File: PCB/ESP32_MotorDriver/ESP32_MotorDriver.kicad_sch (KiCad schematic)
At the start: 39 parts, among them J1 USB_C_Receptacle_USB2.0, J2 Conn_01x06, J4 Conn_01x05, J6 Conn_01x07, J7 Conn_01x17, Q1 SSM3J338R_LF, SW1 EN, SW2 BOOT, U1 ESP32-S2-SOLO-N4, U2 D3V3XA4B10LP, U4 TB6612FNG, U5 AP63203WU

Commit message: actual _v01
Issue with files being copied - these should be good
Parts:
- removed Q1: SSM3J338R_LF, SSM3J338R_LF:SOT-23F_TOS, symbol KiCADv6:SSM3J338R_LF
- removed R10, R9: 4k7, Resistor_SMD:R_0402_1005Metric_Pad0.72x0.64mm_HandSolder, symbol Device:R
- removed U2: D3V3XA4B10LP, Package_DFN_QFN:Diodes_UDFN-10_1x2.5mm_P0.5mm, symbol Power_Protection:D3V3XA4B10LP
- added D3: SMAJ12A, Diode_SMD:D_SMA, symbol Diode:SMAJ12A
- added F2: Polyfuse 500mA, Fuse:Fuse_0805_2012Metric_Pad1.15x1.40mm_HandSolder, symbol Device:Polyfuse
- added Q1: AO3407A, Package_TO_SOT_SMD:SOT-23, symbol Transistor_FET:AO3401A
- added R5, R6: 22R, Resistor_SMD:R_0402_1005Metric_Pad0.72x0.64mm_HandSolder, symbol Device:R_Small
- added U2: USBLC6-2SC6, Package_TO_SOT_SMD:SOT-23-6, symbol Power_Protection:USBLC6-2SC6
- C1, C11, C15, C3, C5, C7: MANUFACTURER (none) -> Samsung Electro-Mechanics; PN_Digikey (none) -> 1276-2891-1-ND; PN_LCSC (none) -> C15850; PN_Manufacturer (none) -> CL21A106KAYNNNE
- C10, C9: MANUFACTURER (none) -> Samsung Electro-Mechanics; PN_Digikey (none) -> 1276-2908-1-ND; PN_LCSC (none) -> C45783; PN_Manufacturer (none) -> CL21A226MAQNNNE
- C12, C13, C14, C2, C4, C6, C8: MANUFACTURER (none) -> Murata; PN_Digikey (none) -> 490-10700-1-ND; PN_LCSC (none) -> C77020; PN_Manufacturer (none) -> GRM155R71H104KE14D
- D1, D2: value D_Schottky -> SS14HE; PN_LCSC (none) -> C894424
- F1: value Polyfuse 4A -> Polyfuse 3A; footprint Fuse:Fuse_0805_2012Metric_Pad1.15x1.40mm_HandSolder -> Fuse:Fuse_1812_4532Metric_Pad1.30x3.40mm_HandSolder; LCSC PN C22368431 -> (none); MANUFACTURER (none) -> Bourns; PN_Digikey MFU08054.00CT-ND -> MF-MSMF250-16X-2CT-ND; PN_LCSC C22368431 -> C210838; PN_Manufacturer MFU0805FF04000P100 -> MF-MSMF250/16X-2
- J1: PN_LCSC (none) -> C165948
- L1: MANUFACTURER (none) -> Murata; Manufacturer Murata Electronics -> (none); PN_LCSC (none) -> C668313
- R1, R2: MANUFACTURER (none) -> Yageo; PN_Digikey (none) -> 311-5.10KLRCT-ND; PN_LCSC (none) -> C25905; PN_Manufacturer (none) -> RC0402FR-075K1L
- R11, R12, R3, R4: MANUFACTURER (none) -> Yageo; PN_Digikey (none) -> 311-10.0KLRCT-ND; PN_LCSC (none) -> C25744; PN_Manufacturer (none) -> RC0402FR-0710KL
- SW1: value EN -> RESET; MANUFACTURER (none) -> Mitsumi; PN_LCSC (none) -> C4364645
- SW2: MANUFACTURER (none) -> Mitsumi; PN_LCSC (none) -> C4364645
- U1: MAXIMUM_PACKAGE_HEIGHT (none) -> 3.25 mm; PN_Manufacturer (none) -> ESP32-S2-SOLO-N4
- U4: MANUFACTURER (none) -> Toshiba
- U5: MANUFACTURER (none) -> Diodes Incorporated; PN_LCSC (none) -> C780769
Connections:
- net GND: now also D3.2 (A2), U2.2 (GND)
- net USB_N: now also R5.1, U2.1 (I/O1), U2.6 (I/O1); no longer U1.13 (IO19)
- net USB_P: now also R6.1, U2.3 (I/O2), U2.4 (I/O2); no longer U1.14 (IO20)
- net VBUS: now also F2.2, U2.5 (VBUS); no longer J1.A4 (VBUS), J1.A9 (VBUS), J1.B4 (VBUS), J1.B9 (VBUS)
- net VM: now also D3.1 (A1)
- net Vbatt: now also Q1.3 (D)
- net at R11.2: now also Q1.1 (G)
- net at F1.1: now also Q1.2 (S)
- net MISO renamed IO12
- net MOSI renamed IO13
- net SCK renamed IO11
- net SCL renamed IO33
- net SDA renamed IO34
- new net: F2.1, J1.A4 (VBUS), J1.A9 (VBUS), J1.B4 (VBUS), J1.B9 (VBUS)
- new net USB_N_ESP: R5.2, U1.13 (IO19)
- new net USB_P_ESP: R6.2, U1.14 (IO20)
- no-connect marks 2 -> 4
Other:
- note removed: "I2C"
- moved on the sheet: R11

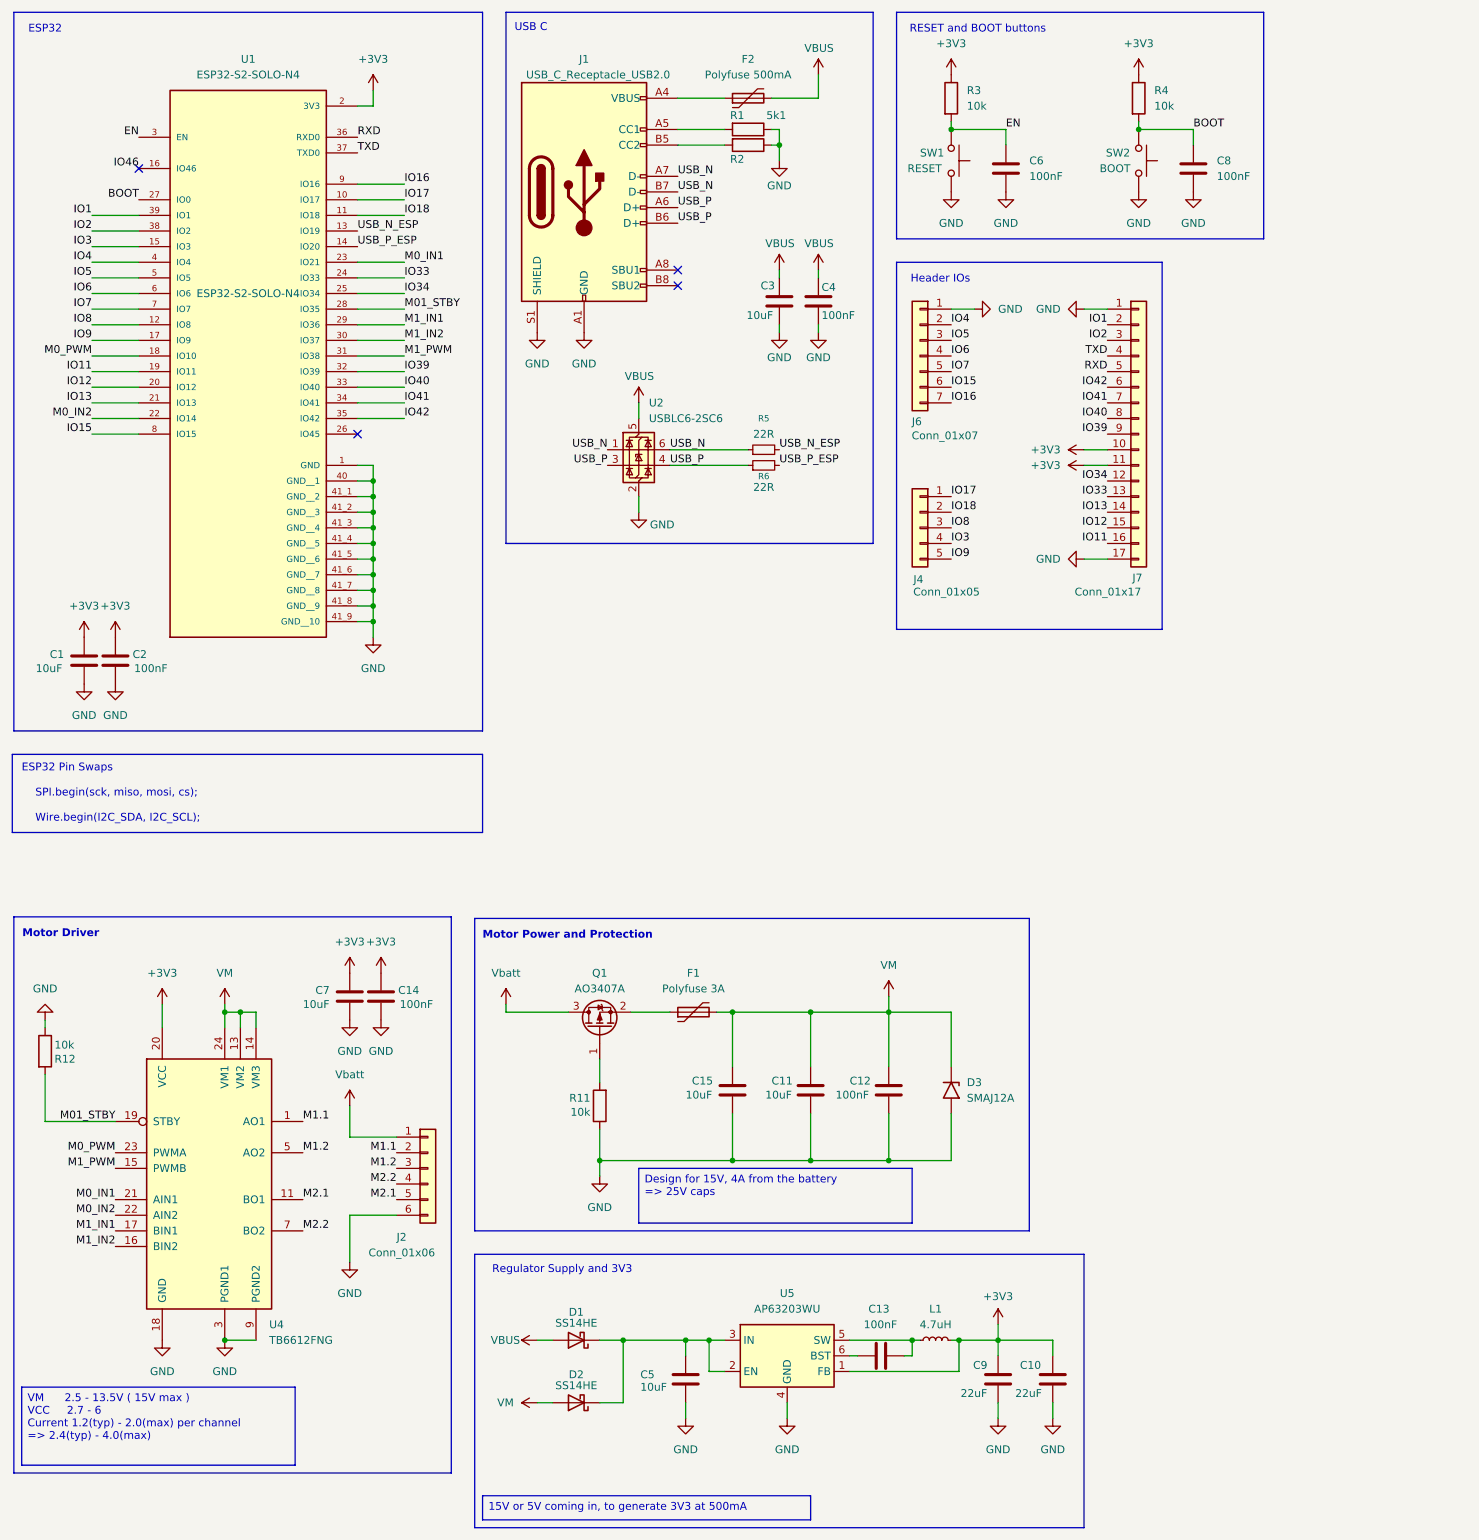
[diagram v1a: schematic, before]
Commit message: BOB v02
Submitted for manufacturer with a few minor fixes from v01. 3V3 to LineFollower array, New footprint for Motor connections and a switch added for power on/off
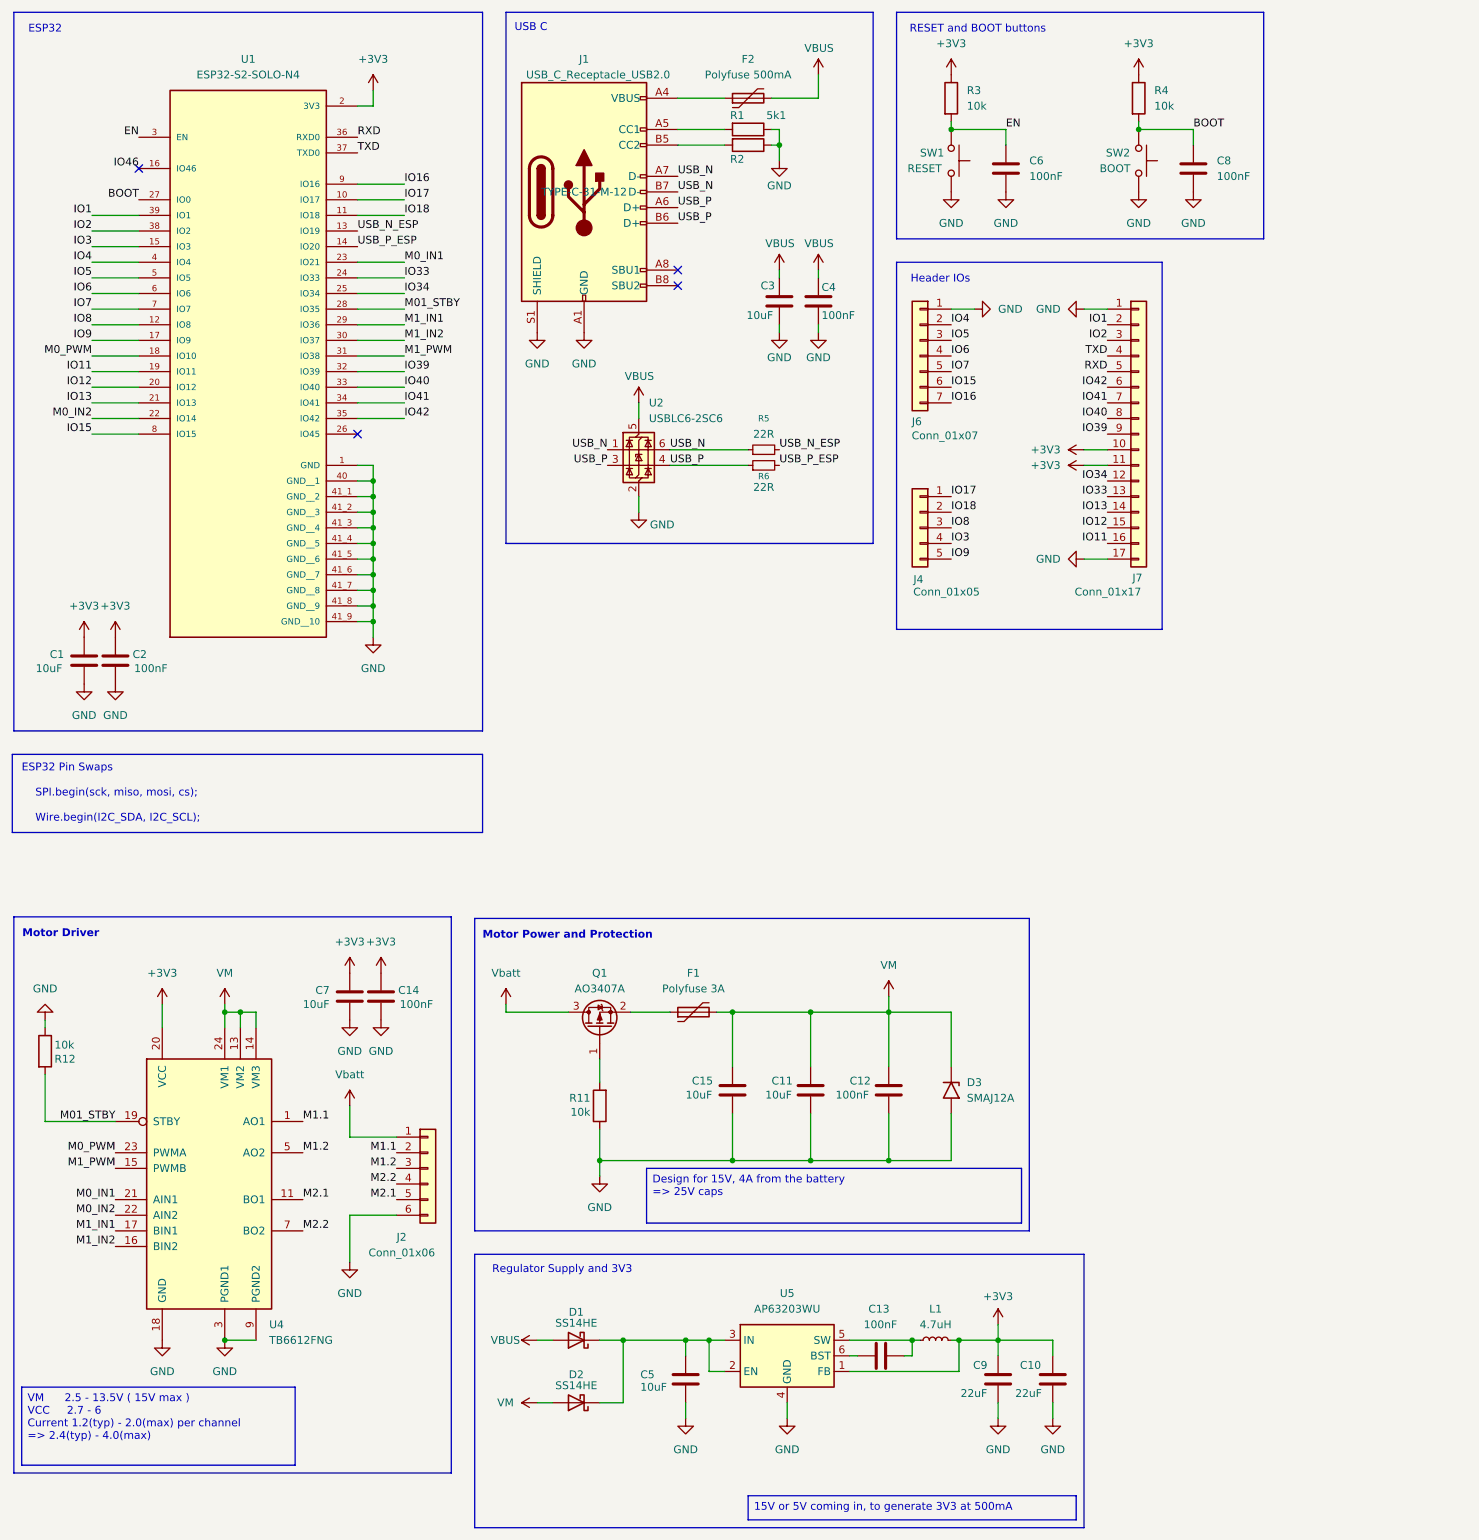
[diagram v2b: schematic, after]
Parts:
- D1, D2: footprint Diode_SMD:D_SOD-323F -> _diodes:D_SOD-323HE_SS14HE
- J1: MANUFACTURER (none) -> Korean Hroparts Elec; PN_Manufacturer (none) -> TYPE-C-31-M-12
- J2: MANUFACTURER (none) -> Adam Tech; PN_Digikey (none) -> 2057-PH1-06-UA-ND; PN_LCSC (none) -> C5845077; PN_Manufacturer (none) -> PH1-06-UA
- J4: MANUFACTURER (none) -> Adam Tech; PN_Digikey (none) -> 2057-PH1-05-UA-ND; PN_LCSC (none) -> C5374051; PN_Manufacturer (none) -> PH1-05-UA
- J6: MANUFACTURER (none) -> Adam Tech; PN_Digikey (none) -> 2057-PH1-07-UA-ND; PN_LCSC (none) -> C3331618; PN_Manufacturer (none) -> PH1-07-UA
- J7: MANUFACTURER (none) -> Adam Tech; PN_Digikey (none) -> 2057-PH1-17-UA-ND; PN_LCSC (none) -> C6251621; PN_Manufacturer (none) -> PH1-17-UA
- L1: MANUFACTURER Murata -> (none)
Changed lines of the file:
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@@
 	(text_box "15V or 5V coming in, to generate 3V3 at 500mA"
 		(exclude_from_sim no)
-		(at 93.98 258.9651 0)
+		(at 137.16 258.9651 0)
 		(size 53.34 3.9249)
 		(margins 0.9525 0.9525 0.9525 0.9525)
@@
 	(text_box "Design for 15V, 4A from the battery\n => 25V caps"
 		(exclude_from_sim no)
-		(at 119.38 205.74 0)
-		(size 44.45 8.89)
+		(at 120.65 205.74 0)
+		(size 60.96 8.89)
 		(margins 0.9525 0.9525 0.9525 0.9525)
 		(stroke
@@
 			)
 		)
-		(property "PN_Manufacturer" ""
+		(property "PN_Manufacturer" "TYPE-C-31-M-12"
 			(at 110.49 46.99 0)
 			(show_name no)
@@
 			)
 		)
+		(property "MANUFACTURER" "Korean Hroparts Elec"
+			(at 110.49 46.99 0)
+			(hide yes)
+			(show_name no)
+			(do_not_autoplace no)
+			(effects
+				(font
+					(size 1.27 1.27)
+				)
+			)
+		)
 		(pin "A1"
 		)
@@
 			)
 		)
-		(property "MANUFACTURER" "Murata"
-			(at 167.64 233.68 90)
-			(hide yes)
-			(show_name no)
-			(do_not_autoplace no)
-			(effects
-				(font
-					(size 1.27 1.27)
-				)
-			)
-		)
 		(pin "1"
 		)
@@
 			)
 		)
-		(property "Footprint" "Diode_SMD:D_SOD-323F"
+		(property "Footprint" "_diodes:D_SOD-323HE_SS14HE"
 			(at 109.22 243.84 0)
 			(hide yes)
@@
 			)
 		)
-		(property "PN_Manufacturer" ""
+		(property "PN_Manufacturer" "PH1-06-UA"
 			(at 85.09 205.74 0)
+			(hide yes)
 			(show_name no)
 			(do_not_autoplace no)
@@
 			)
 		)
-		(property "PN_Digikey" ""
+		(property "PN_Digikey" "2057-PH1-06-UA-ND"
 			(at 85.09 205.74 0)
 			(hide yes)
@@
 			)
 		)
+		(property "MANUFACTURER" "Adam Tech"
+			(at 85.09 205.74 0)
+			(hide yes)
+			(show_name no)
+			(do_not_autoplace no)
+			(effects
+				(font
+					(size 1.27 1.27)
+				)
+			)
+		)
+		(property "PN_LCSC" "C5845077"
+			(at 85.09 205.74 0)
+			(hide yes)
+			(show_name no)
+			(do_not_autoplace no)
+			(effects
+				(font
+					(size 1.27 1.27)
+				)
+			)
+		)
 		(pin "6"
 		)
@@
 			)
 		)
-		(property "PN_Manufacturer" ""
+		(property "PN_Manufacturer" "PH1-05-UA"
 			(at 165.1 101.6 0)
+			(hide yes)
 			(show_name no)
 			(do_not_autoplace no)
@@
 			)
 		)
-		(property "PN_Digikey" ""
+		(property "PN_Digikey" "2057-PH1-05-UA-ND"
+			(at 165.1 101.6 0)
+			(hide yes)
+			(show_name no)
+			(do_not_autoplace no)
+			(effects
+				(font
+					(size 1.27 1.27)
+				)
+			)
+		)
+		(property "MANUFACTURER" "Adam Tech"
+			(at 165.1 101.6 0)
+			(hide yes)
+			(show_name no)
+			(do_not_autoplace no)
+			(effects
+				(font
+					(size 1.27 1.27)
+				)
+			)
+		)
+		(property "PN_LCSC" "C5374051"
 			(at 165.1 101.6 0)
 			(hide yes)
@@
 			)
 		)
-		(property "PN_Manufacturer" ""
+		(property "PN_Manufacturer" "PH1-07-UA"
 			(at 165.1 73.66 0)
+			(hide yes)
 			(show_name no)
 			(do_not_autoplace no)
@@
 			)
 		)
-		(property "PN_Digikey" ""
+		(property "PN_Digikey" "2057-PH1-07-UA-ND"
 			(at 165.1 73.66 0)
 			(hide yes)
@@
 			)
 		)
+		(property "MANUFACTURER" "Adam Tech"
+			(at 165.1 73.66 0)
+			(hide yes)
+			(show_name no)
+			(do_not_autoplace no)
+			(effects
+				(font
+					(size 1.27 1.27)
+				)
+			)
+		)
+		(property "PN_LCSC" "C3331618"
+			(at 165.1 73.66 0)
+			(hide yes)
+			(show_name no)
+			(do_not_autoplace no)
+			(effects
+				(font
+					(size 1.27 1.27)
+				)
+			)
+		)
 		(pin "1"
 		)
@@
 			)
 		)
-		(property "Footprint" "Diode_SMD:D_SOD-323F"
+		(property "Footprint" "_diodes:D_SOD-323HE_SS14HE"
 			(at 109.22 233.68 0)
 			(hide yes)
@@
 			)
 		)
-		(property "PN_Manufacturer" ""
+		(property "PN_Manufacturer" "PH1-17-UA"
 			(at 200.66 86.36 0)
+			(hide yes)
 			(show_name no)
 			(do_not_autoplace no)
@@
 			)
 		)
-		(property "PN_Digikey" ""
+		(property "PN_Digikey" "2057-PH1-17-UA-ND"
+			(at 200.66 86.36 0)
+			(hide yes)
+			(show_name no)
+			(do_not_autoplace no)
+			(effects
+				(font
+					(size 1.27 1.27)
+				)
+			)
+		)
+		(property "MANUFACTURER" "Adam Tech"
+			(at 200.66 86.36 0)
+			(hide yes)
+			(show_name no)
+			(do_not_autoplace no)
+			(effects
+				(font
+					(size 1.27 1.27)
+				)
+			)
+		)
+		(property "PN_LCSC" "C6251621"
 			(at 200.66 86.36 0)
 			(hide yes)
@@
 		(property "PN_Manufacturer" "ESP32-S2-SOLO-N4"
 			(at 55.88 63.5 0)
+			(hide yes)
 			(show_name no)
 			(do_not_autoplace no)
@@
 			(at 113.03 195.58 0)
 			(hide yes)
-			(show_name no)
-			(do_not_autoplace no)
-			(effects
-				(font
-					(size 1.27 1.27)
-				)
-			)
-		)
-		(property "Supplier" ""
-			(at 113.03 195.58 0)
-			(hide yes)
-			(show_name no)
-			(do_not_autoplace no)
-			(effects
-				(font
-					(size 1.27 1.27)
-				)
-			)
-		)
-		(property "PN_Digikey_150mA" ""
-			(at 113.03 195.58 0)
-			(hide yes)
-			(show_name no)
-			(do_not_autoplace no)
-			(effects
-				(font
-					(size 1.27 1.27)
-				)
-			)
-		)
-		(property "PN_Digikey_600mA" ""
-			(at 113.03 195.58 0)
-			(hide yes)
